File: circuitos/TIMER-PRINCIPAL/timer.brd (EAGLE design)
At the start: 91.1 x 38.1 mm, 19 parts, among them IC1 MEGA8-P, IC2 7805TV, J1 PWR, K1 JJM1-12V, Q1 16Mhz, T1 BC337, X1 IN, X2 OUT, X3 BOTOEIRA

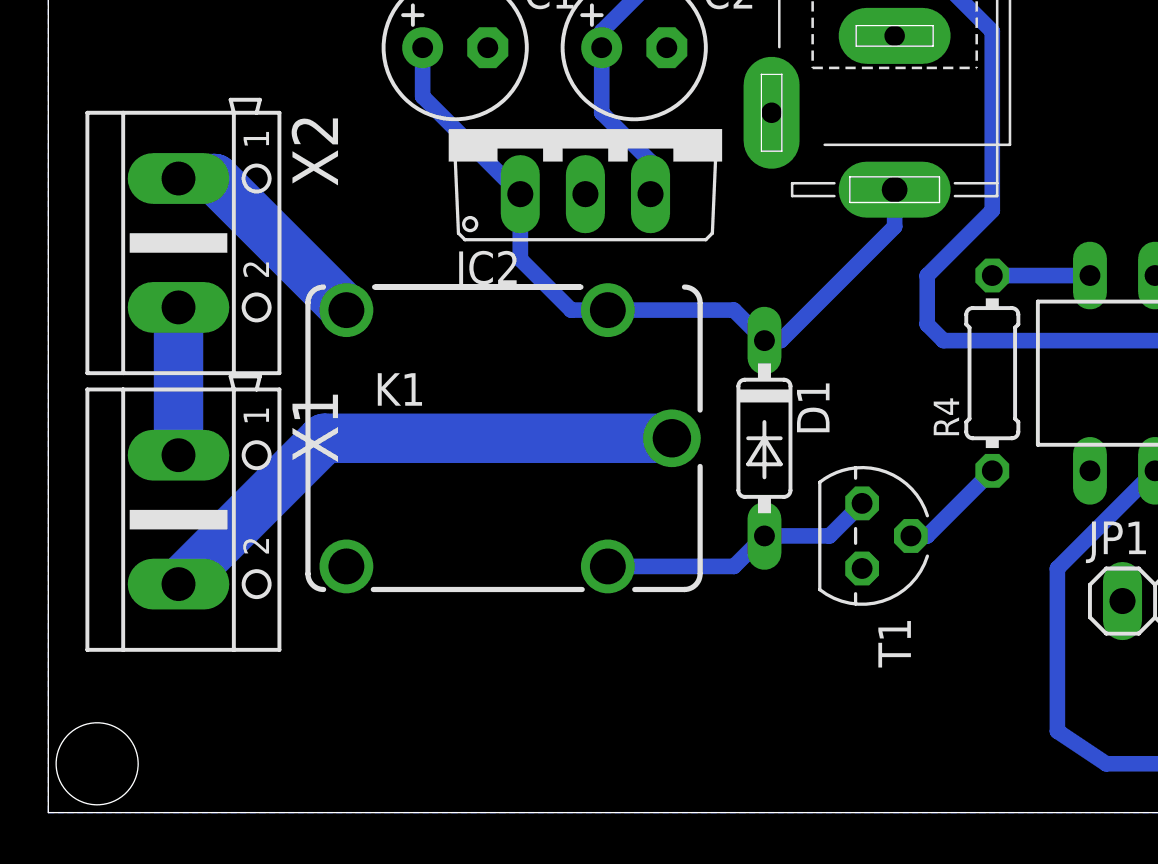
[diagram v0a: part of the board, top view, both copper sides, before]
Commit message: Trocado o componente do relé
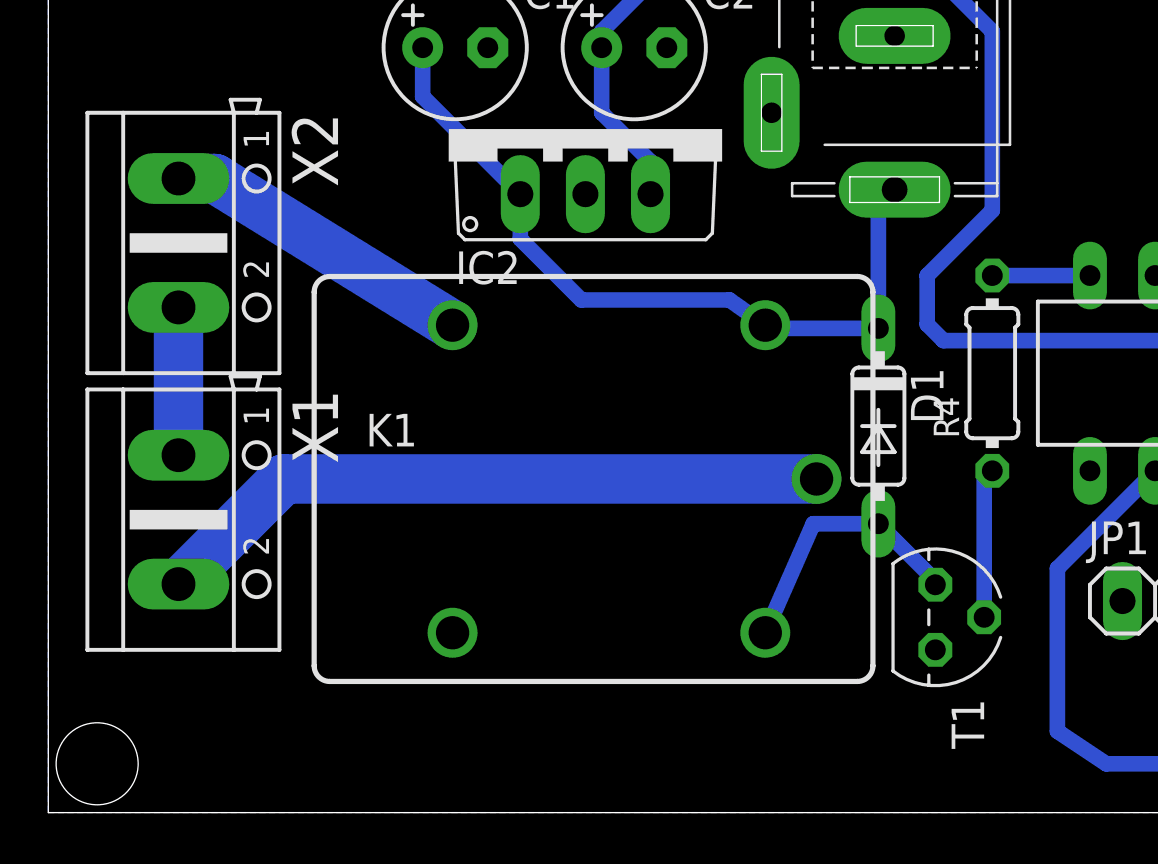
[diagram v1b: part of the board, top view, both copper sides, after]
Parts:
- K1: value JJM1-12V -> JS-M1-12V-4; device relay:JJM1C -> relay:JS-M
- moved D1 4.47 mm to (32.4, 15.1)
- moved T1 4.27 mm to (34.6, 7.62)
- moved K1 3.84 mm to (21.3, 13.0)
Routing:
- net N$3: track 21.6 -> 26.6 mm
- net N$2: track 8.68 -> 12.3 mm
- net N$18: track 4.23 -> 6.03 mm
- net VDD: track 29.0 -> 30.0 mm
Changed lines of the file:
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@@
 <setting verticaltext="up"/>
 </settings>
-<grid distance="6.25" unitdist="mil" unit="mm" style="lines" multiple="1" display="no" altdistance="6.25" altunitdist="mil" altunit="mil"/>
+<grid distance="6.25" unitdist="mil" unit="mil" style="lines" multiple="1" display="no" altdistance="6.25" altunitdist="mil" altunit="mil"/>
 <layers>
-<layer number="1" name="Top" color="4" fill="1" visible="no" active="yes"/>
+<layer number="1" name="Top" color="4" fill="1" visible="yes" active="yes"/>
 <layer number="16" name="Bottom" color="1" fill="1" visible="yes" active="yes"/>
 <layer number="17" name="Pads" color="2" fill="1" visible="yes" active="yes"/>
@@
 <layer number="19" name="Unrouted" color="6" fill="1" visible="yes" active="yes"/>
 <layer number="20" name="Dimension" color="15" fill="1" visible="yes" active="yes"/>
-<layer number="21" name="tPlace" color="7" fill="1" visible="no" active="yes"/>
-<layer number="22" name="bPlace" color="7" fill="1" visible="no" active="yes"/>
-<layer number="23" name="tOrigins" color="15" fill="1" visible="no" active="yes"/>
-<layer number="24" name="bOrigins" color="15" fill="1" visible="no" active="yes"/>
-<layer number="25" name="tNames" color="7" fill="1" visible="no" active="yes"/>
-<layer number="26" name="bNames" color="7" fill="1" visible="no" active="yes"/>
-<layer number="27" name="tValues" color="7" fill="1" visible="no" active="yes"/>
-<layer number="28" name="bValues" color="7" fill="1" visible="no" active="yes"/>
+<layer number="21" name="tPlace" color="7" fill="1" visible="yes" active="yes"/>
+<layer number="22" name="bPlace" color="7" fill="1" visible="yes" active="yes"/>
+<layer number="23" name="tOrigins" color="15" fill="1" visible="yes" active="yes"/>
+<layer number="24" name="bOrigins" color="15" fill="1" visible="yes" active="yes"/>
+<layer number="25" name="tNames" color="7" fill="1" visible="yes" active="yes"/>
+<layer number="26" name="bNames" color="7" fill="1" visible="yes" active="yes"/>
+<layer number="27" name="tValues" color="7" fill="1" visible="yes" active="yes"/>
+<layer number="28" name="bValues" color="7" fill="1" visible="yes" active="yes"/>
 <layer number="29" name="tStop" color="7" fill="3" visible="no" active="yes"/>
 <layer number="30" name="bStop" color="7" fill="6" visible="no" active="yes"/>
@@
 </element>
 <element name="R1" library="rcl" package="0204/7" value="10k" x="77.47" y="17.145" rot="R90"/>
-<element name="K1" library="relay" package="JJM1C" value="JJM1-12V" x="17.78" y="14.605">
-<attribute name="OC_NEWARK" value="10C7318" x="54.61" y="-52.705" size="1.778" layer="27" display="off"/>
-<attribute name="MPN" value="JJM1-12V" x="54.61" y="-52.705" size="1.778" layer="27" display="off"/>
-<attribute name="MF" value="AROMAT/ MATSUSHITA" x="54.61" y="-52.705" size="1.778" layer="27" display="off"/>
-<attribute name="OC_FARNELL" value="unknown" x="54.61" y="-52.705" size="1.778" layer="27" display="off"/>
-</element>
-<element name="T1" library="transistor" package="TO92" value="BC337" x="31.75" y="10.795" rot="R270"/>
-<element name="D1" library="diode" package="DO35-7" value="1N4148DO35-7" x="27.94" y="14.605" rot="R270"/>
+<element name="K1" library="relay" package="JS-M" value="JS-M1-12V-4" x="21.2725" y="13.0175">
+<attribute name="OC_NEWARK" value="13P4552" x="58.1025" y="-54.2925" size="1.778" layer="27" display="off"/>
+<attribute name="MPN" value="JSM1-12V-4" x="58.1025" y="-54.2925" size="1.778" layer="27" display="off"/>
+<attribute name="MF" value="" x="58.1025" y="-54.2925" size="1.778" layer="27" display="off"/>
+<attribute name="OC_FARNELL" value="910338" x="58.1025" y="-54.2925" size="1.778" layer="27" display="off"/>
+</element>
+<element name="T1" library="transistor" package="TO92" value="BC337" x="34.6075" y="7.62" rot="R270"/>
+<element name="D1" library="diode" package="DO35-7" value="1N4148DO35-7" x="32.385" y="15.08125" rot="R270"/>
 <element name="R4" library="rcl" package="0204/7" value="2,2K" x="36.83" y="17.145" rot="R90"/>
 <element name="JP1" library="pinhead" package="1X06" value="ISP" x="48.26" y="8.255"/>
@@
 <contactref element="K1" pad="1"/>
 <contactref element="D1" pad="C"/>
-<wire x1="21.83" y1="19.605" x2="20.4" y2="19.605" width="0.6096" layer="16"/>
-<wire x1="20.4" y1="19.605" x2="18.415" y2="21.59" width="0.6096" layer="16"/>
-<wire x1="18.415" y1="21.59" x2="18.415" y2="24.13" width="0.6096" layer="16"/>
 <wire x1="14.605" y1="29.845" x2="14.605" y2="27.94" width="0.6096" layer="16"/>
 <wire x1="14.605" y1="27.94" x2="18.415" y2="24.13" width="0.6096" layer="16"/>
-<wire x1="21.83" y1="19.605" x2="26.75" y2="19.605" width="0.6096" layer="16"/>
-<wire x1="26.75" y1="19.605" x2="27.94" y2="18.415" width="0.6096" layer="16"/>
-<wire x1="27.94" y1="18.415" x2="28.575" y2="18.415" width="0.6096" layer="16"/>
-<wire x1="28.575" y1="18.415" x2="33.02" y2="22.86" width="0.6096" layer="16"/>
-<wire x1="33.02" y1="22.86" x2="33.02" y2="24.305" width="0.6096" layer="16"/>
+<wire x1="18.415" y1="24.13" x2="18.415" y2="22.38375" width="0.6096" layer="16"/>
+<wire x1="18.415" y1="22.38375" x2="20.79625" y2="20.0025" width="0.6096" layer="16"/>
+<wire x1="20.79625" y1="20.0025" x2="26.57625" y2="20.0025" width="0.6096" layer="16"/>
+<wire x1="26.57625" y1="20.0025" x2="27.9725" y2="19.0175" width="0.6096" layer="16"/>
+<wire x1="33.02" y1="24.305" x2="32.385" y2="23.67" width="0.6096" layer="16"/>
+<wire x1="32.385" y1="23.67" x2="32.385" y2="18.89125" width="0.6096" layer="16"/>
+<wire x1="27.9725" y1="19.0175" x2="28.2575" y2="18.89125" width="0.6096" layer="16"/>
+<wire x1="28.2575" y1="18.89125" x2="32.385" y2="18.89125" width="0.6096" layer="16"/>
 </signal>
 <signal name="N$17">
@@
 <contactref element="T1" pad="3"/>
 <contactref element="D1" pad="A"/>
-<wire x1="21.83" y1="9.605" x2="26.75" y2="9.605" width="0.6096" layer="16"/>
-<wire x1="26.75" y1="9.605" x2="27.94" y2="10.795" width="0.6096" layer="16"/>
-<wire x1="27.94" y1="10.795" x2="30.48" y2="10.795" width="0.6096" layer="16"/>
-<wire x1="30.48" y1="10.795" x2="31.75" y2="12.065" width="0.6096" layer="16"/>
+<wire x1="27.9725" y1="7.0175" x2="29.845" y2="11.27125" width="0.6096" layer="16"/>
+<wire x1="29.845" y1="11.27125" x2="32.385" y2="11.27125" width="0.6096" layer="16"/>
+<wire x1="32.385" y1="11.27125" x2="34.6075" y2="9.04875" width="0.6096" layer="16"/>
+<wire x1="34.6075" y1="9.04875" x2="34.6075" y2="8.89" width="0.6096" layer="16"/>
 </signal>
 <signal name="N$18">
 <contactref element="T1" pad="2"/>
 <contactref element="R4" pad="1"/>
-<wire x1="33.655" y1="10.795" x2="34.29" y2="10.795" width="0.6096" layer="16"/>
-<wire x1="34.29" y1="10.795" x2="36.83" y2="13.335" width="0.6096" layer="16"/>
+<wire x1="36.83" y1="13.335" x2="36.5125" y2="13.335" width="0.6096" layer="16"/>
+<wire x1="36.5125" y1="13.335" x2="36.5125" y2="7.62" width="0.6096" layer="16"/>
 </signal>
 <signal name="N$19">
@@
 <contactref element="K1" pad="NO"/>
 <wire x1="5.08" y1="24.7396" x2="6.4954" y2="24.7396" width="1.9304" layer="16"/>
-<wire x1="6.4954" y1="24.7396" x2="11.63" y2="19.605" width="1.9304" layer="16"/>
+<wire x1="6.4954" y1="24.7396" x2="15.7725" y2="19.0175" width="1.9304" layer="16"/>
 </signal>
 <signal name="N$3">
 <contactref element="K1" pad="C"/>
 <contactref element="X1" pad="2"/>
-<wire x1="24.33" y1="14.605" x2="10.7696" y2="14.605" width="1.9304" layer="16"/>
-<wire x1="10.7696" y1="14.605" x2="5.08" y2="8.9154" width="1.9304" layer="16"/>
+<wire x1="5.08" y1="8.9154" x2="9.1821" y2="13.0175" width="1.9304" layer="16"/>
+<wire x1="9.1821" y1="13.0175" x2="29.9725" y2="13.0175" width="1.9304" layer="16"/>
 </signal>
 <signal name="N$21">
